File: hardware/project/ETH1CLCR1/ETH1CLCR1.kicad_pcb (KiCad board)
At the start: 8 copper layers, 160 x 100 mm, 732 parts, among them J1201 C64AC, J1301 20021111-00010T4LF, J301 Conn_02x01, J302 20021111-00010T4LF, J601 20021111-00010T4LF, K1201 HE3621A0510, K1202 HE3621A0510, K1203 HE3621A0510, K1204 HE3621A0510, K1205 HE3621A0510, K1206 HE3621A0510, K701 9012, K702 9012, K703 9012, K704 9012, K801 TQ2SA-5V, Q1101 BC847W, Q1102 BC847W, Q1103 BC847W, Q1104 BC847W, Q501 IRFR5410, Q701 BC847W, Q702 BC847W, Q703 BC847W, Q704 BC847W, Q705 MMBT4401L, Q706 MMBT4403L, Q801 BC847W, Q802 2N2218A, Q803 2N2904A, Q804 BC847W, Q805 BC847W, Q806 BC847W, Q807 BC847W, Q808 BC847W, Q901 BC847W, Q902 BC847W, Q903 BC847W, U1001 TL074, U1002 TL074, U1003 REF192, U1004 DAC8568IBPWR, U1101 ADG419BR, U1102 ADG419BR, U1103 REF192, U1104 AD8606-2-MSOP, U1105 AD8606-2-MSOP, U1106 AD7380, U1107 AD8605, U1108 LT6350, U1109 LT6350, U1110 OPA602, U1111 OPA602, U1112 PGA103, U1113 PGA103, U1201 ULN2003A, U1301 24LC08B-E/MS, U1302 STM32H743ZI, U1401 ECS-3225SMV-500-GP-TR, U1402 REF192, U1403 74AHCT1G08, U1404 AD5689BRUZ, U1405 AD9835, U1406 TL072, U1407 DG419LDY, U1408 AD5453YRMZ, U1409 LT1468, U1410 LT1468, U1411 LT1468, U1501 TSR2-2450, U1502 LM1117DTX-3.3/NOPB, U1503 LM1117DTX-3.3/NOPB, U1504 LT8330_S6, U1505 LT8330_S6, U1506 MC7815BD2TG, U1507 MC7915BD2TG, U1508 TSR1-2490, U1509 LM1117DTX-5.0/NOPB, U1510 MC78M12ABDTRKG, U1511 MC79M12CDTG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

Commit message: PCB layout
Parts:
- added C1115: 100n, Capacitor_SMD:C_0603_1608Metric_Pad1.05x0.95mm_HandSolder, B.Cu at (92.2, 78.2)
- added C1117: 100n, Capacitor_SMD:C_0603_1608Metric_Pad1.05x0.95mm_HandSolder, B.Cu at (92.2, 75.7)
- added C1119: 100n, Capacitor_SMD:C_0603_1608Metric_Pad1.05x0.95mm_HandSolder, B.Cu at (102.6, 79.2)
- added C1123: 100n, Capacitor_SMD:C_0603_1608Metric_Pad1.05x0.95mm_HandSolder, B.Cu at (115.1, 77.0)
- added C1125: 100n, Capacitor_SMD:C_0603_1608Metric_Pad1.05x0.95mm_HandSolder, B.Cu at (92.2, 71.9)
- added C1127: 100n, Capacitor_SMD:C_0603_1608Metric_Pad1.05x0.95mm_HandSolder, B.Cu at (102.6, 77.0)
- added C1129: 100n, Capacitor_SMD:C_0603_1608Metric_Pad1.05x0.95mm_HandSolder, B.Cu at (115.1, 79.2)
- added C1131: 100n, Capacitor_SMD:C_0603_1608Metric_Pad1.05x0.95mm_HandSolder, B.Cu at (92.2, 69.3)
- moved TP1501 31.9 mm to (82.8, 82.9)
- moved C1523 2.44 mm to (83.1, 114.8)
- moved C1520 2.33 mm to (86.2, 114.8)
- moved C1525 1.27 mm to (88.8, 119.8)
- moved C1528 1.27 mm to (92.3, 48.6)
- moved U1511 1.02 mm to (88.9, 48.6)
- moved C1524 0.89 mm to (109.0, 114.8)
- moved D1502 0.76 mm to (103.9, 121.5)
- moved C1519 0.64 mm to (103.9, 114.8)
- moved C1522 0.64 mm to (100.8, 114.8)
- moved C1512 0.51 mm to (111.1, 134.7)
- moved C1514 0.51 mm to (105.9, 127.3)
- moved C1515 0.51 mm to (91.2, 127.6)
- moved C1516 0.51 mm to (101.9, 134.7)
- moved D1501 0.51 mm to (95.1, 132.0)
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- renumbered C1115 to C1116, C1116 to C1118, C1117 to C1120, C1118 to C1121, C1119 to C1122, C1120 to C1124, C1121 to C1126, C1122 to C1128, C1123 to C1130, C1124 to C1132, C1125 to C1133, C1126 to C1134, C1127 to C1135, C1128 to C1136, C1129 to C1137, C1130 to C1138, R1141 to R1139, R1142 to R1140, R1139 to R1141, R1140 to R1142
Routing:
- net -15VF: track 0.00 -> 37.4 mm, vias 0 -> 23
- net +15VF: track 0.00 -> 29.2 mm, vias 0 -> 19
- net Net-(C1517-Pad1): track 0.00 -> 25.9 mm, vias 0 -> 13
- net +12VF: track 0.00 -> 16.2 mm, vias 0 -> 11
- net -12VF: track 0.00 -> 13.2 mm, vias 0 -> 9
- net Net-(D812-Pad2): track 0.00 -> 7.16 mm, vias 0 -> 1
- net Net-(C1526-Pad1): track 0.00 -> 6.85 mm, vias 0 -> 5
- net Net-(D701-Pad2): track 0.00 -> 4.70 mm
- net Net-(D702-Pad2): track 0.00 -> 4.54 mm
- net Net-(D703-Pad2): track 0.00 -> 4.52 mm
- net +5VF: track 23.4 -> 27.7 mm, vias 15 -> 17
- net Net-(C1505-Pad1): track 7.25 -> 10.5 mm, vias 5 -> 7
- net Net-(C818-Pad1): track 0.00 -> 3.25 mm
- net Net-(C1517-Pad2): track 0.00 -> 2.41 mm
- net Net-(D704-Pad2): track 0.00 -> 2.22 mm
- added copper zone on F.Cu, net (none)
- added copper zone on B.Cu, net +12VF
- added copper zone on F.Cu, net +12VF
- added copper zone on Power_B, net +12VF
- added copper zone on B.Cu, net +15VF
- added copper zone on F.Cu, net +15VF
- added copper zone on Power_B, net +15VF
- added copper zone on Power_C, net +24VDD
- added copper zone on Power_B, net +3.3VF
- added copper zone on Power_A, net +3.3VP
- added copper zone on Power_B, net +5VF
- added copper zone on Power_B, net +5V_TRIG
- added copper zone on Power_C, net +5V_TRIG
- added copper zone on B.Cu, net -12VF
- added copper zone on F.Cu, net -12VF
- added copper zone on Power_C, net -12VF
- added copper zone on B.Cu, net -15VF
- added copper zone on F.Cu, net -15VF
- added copper zone on Power_C, net -15VF
- added copper zone on B.Cu, net GND_TRIG
- added copper zone on F.Cu, net GND_TRIG
- added copper zone on GNB_B, net GND_TRIG
- added copper zone on Power_A, net Net-(C1505-Pad1)
- added copper zone on Power_B, net Net-(C1505-Pad1)
- added copper zone on Power_C, net Net-(C1505-Pad1)
- added copper zone on B.Cu, net Net-(C1516-Pad1)
- added copper zone on F.Cu, net Net-(C1516-Pad1)
- added copper zone on B.Cu, net Net-(C1517-Pad1)
- added copper zone on F.Cu, net Net-(C1517-Pad1)
- added copper zone on B.Cu, net Net-(C1526-Pad1)
- added copper zone on F.Cu, net Net-(C1526-Pad1)
- added copper zone on Power_A, net Net-(C1526-Pad1)
- added copper zone on Power_B, net Net-(C1526-Pad1)
- removed copper zone on Mixed, net +24VDD
- removed copper zone on Mixed, net Net-(C1505-Pad1)

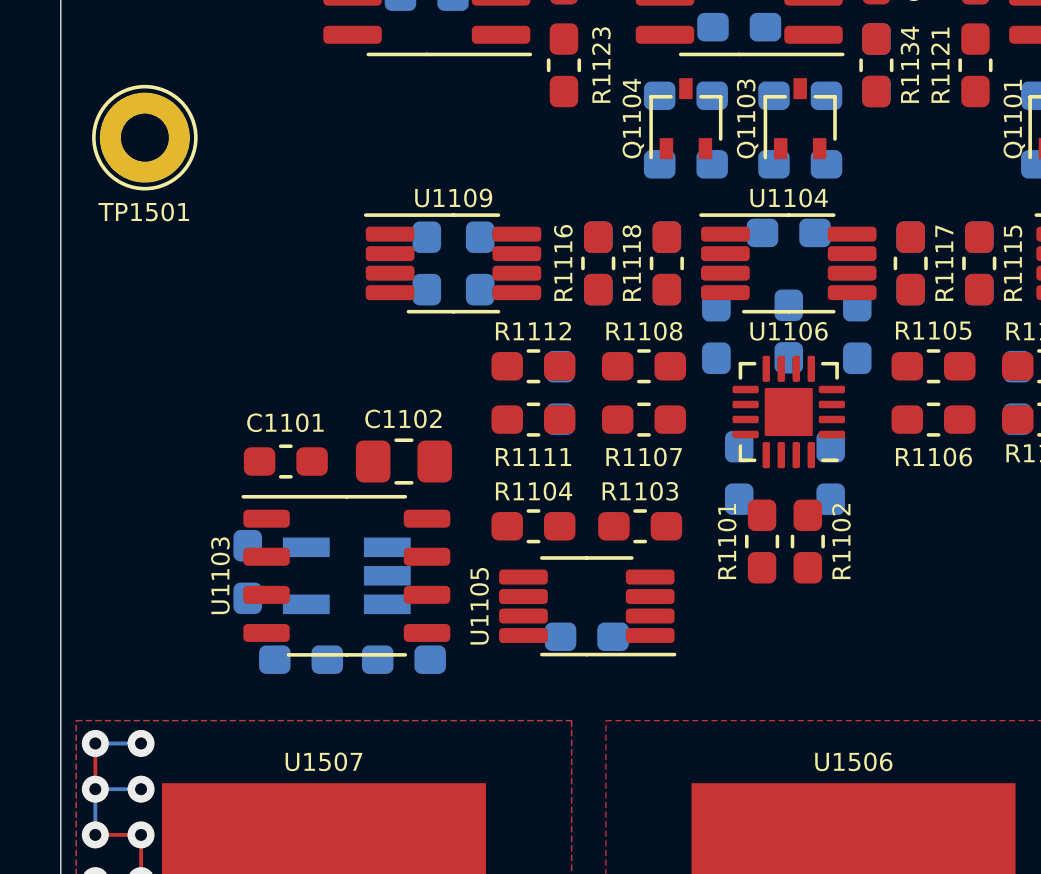
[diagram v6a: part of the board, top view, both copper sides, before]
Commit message: Changed op-amps in ADC schematic.
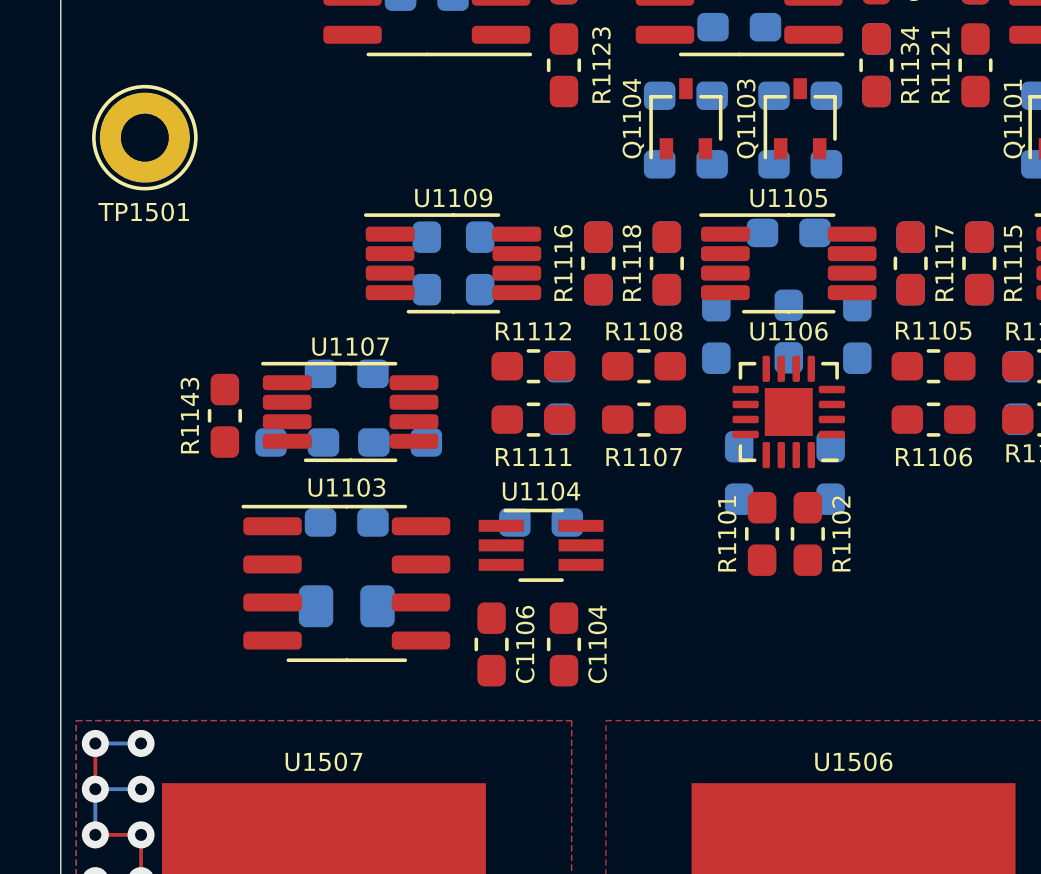
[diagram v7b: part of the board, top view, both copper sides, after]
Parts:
- added R1143: 1M, Resistor_SMD:R_0603_1608Metric_Pad1.05x0.95mm_HandSolder, F.Cu at (85.5, 92.2)
- C1101, C1102: moved to B.Cu
- C1104, C1106: moved to F.Cu
- R1103, R1104: value 10k -> 590; moved to B.Cu
- U1103: value REF192 -> ADR4525BRZ; footprint Package_SO:SSOP-8_3.9x5.05mm_P1.27mm -> Package_SO:SOIC-8_3.9x4.9mm_P1.27mm
- U1104: value AD8606-2-MSOP -> ADA4807-1AKSZ-R2; footprint Package_SO:MSOP-8_3x3mm_P0.65mm -> Package_TO_SOT_SMD:SOT-363_SC-70-6_Handsoldering
- U1105: value AD8606-2-MSOP -> ADA4807-2ARM
- U1107: value AD8605 -> ADA4807-2ARM; footprint Package_TO_SOT_SMD:SOT-23-5_HandSoldering -> Package_SO:MSOP-8_3x3mm_P0.65mm; moved to F.Cu
- moved U1105 13.3 mm to (104.3, 87.1), turned to 0 degrees
- moved U1104 12.5 mm to (96.0, 96.5)
- moved C1124 11.9 mm to (89.5, 90.8), turned to 180 degrees
- moved R1103 11.8 mm to (87.9, 93.1), turned to 180 degrees
- moved C1120 9.92 mm to (96.0, 95.8), turned to 180 degrees
- moved C1106 6.37 mm to (94.4, 99.8), turned to 270 degrees
- moved U1107 5.46 mm to (89.7, 92.1), turned to 0 degrees
- moved C1104 5.36 mm to (96.8, 99.8), turned to 270 degrees
- moved R1104 5.25 mm to (91.3, 93.1), turned to 0 degrees
- moved C1102 5.19 mm to (89.5, 98.6)
- moved C1101 2.87 mm to (89.5, 95.8), turned to 0 degrees
- moved R1101 0.25 mm to (103.4, 96.1)
- moved R1102 0.25 mm to (104.9, 96.1)
- moved U1103 0.25 mm to (89.5, 97.8)
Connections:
- C1104 pad 1: Net-(C1104-Pad1) -> /ADC/REF2V5
- C1106 pad 1: Net-(C1104-Pad1) -> /ADC/REF2V5
- R1103 pad 2: /ADC/REFIO -> /ADC/REF2V5
- U1103 pad 3: +5VF -> (no net)
- U1103 pad 6: Net-(C1104-Pad1) -> /ADC/REF2V5
- U1104 pad 1: Net-(R1116-Pad1) -> /ADC/REFIO
- U1104 pad 2: Net-(R1118-Pad1) -> AGNDF
- U1104 pad 3: Net-(R1123-Pad2) -> /ADC/REF2V5
- U1104 pad 4: AGNDF -> /ADC/REFIO
- U1104 pad 5: Net-(R1121-Pad2) -> +5VF
- U1104 pad 6: Net-(R1117-Pad1) -> +5VF
- U1105 pad 1: /ADC/ADC_REF -> Net-(R1116-Pad1)
- U1105 pad 2: /ADC/ADC_REF -> Net-(R1118-Pad1)
- U1105 pad 3: /ADC/REFIO -> Net-(R1123-Pad2)
- U1105 pad 5: Net-(R1103-Pad1) -> Net-(R1121-Pad2)
- U1105 pad 6: /ADC/VCM -> Net-(R1117-Pad1)
- U1105 pad 7: /ADC/VCM -> Net-(R1115-Pad1)
- U1107 pad 1: /ADC/REFIO -> /ADC/ADC_REF
- U1107 pad 2: AGNDF -> /ADC/ADC_REF
- U1107 pad 3: Net-(C1104-Pad1) -> /ADC/REF2V5
- U1107 pad 4: /ADC/REFIO -> AGNDF
- U1107 pad 5: +5VF -> Net-(R1103-Pad1)
